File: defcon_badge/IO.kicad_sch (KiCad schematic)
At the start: 9 parts, among them J30 SAO 2x3, J31 microSD, J32 UART debug, SW20 TS-1187A, SW21 TS-1187A, SW22 TS-1187A, SW23 TS-1187A

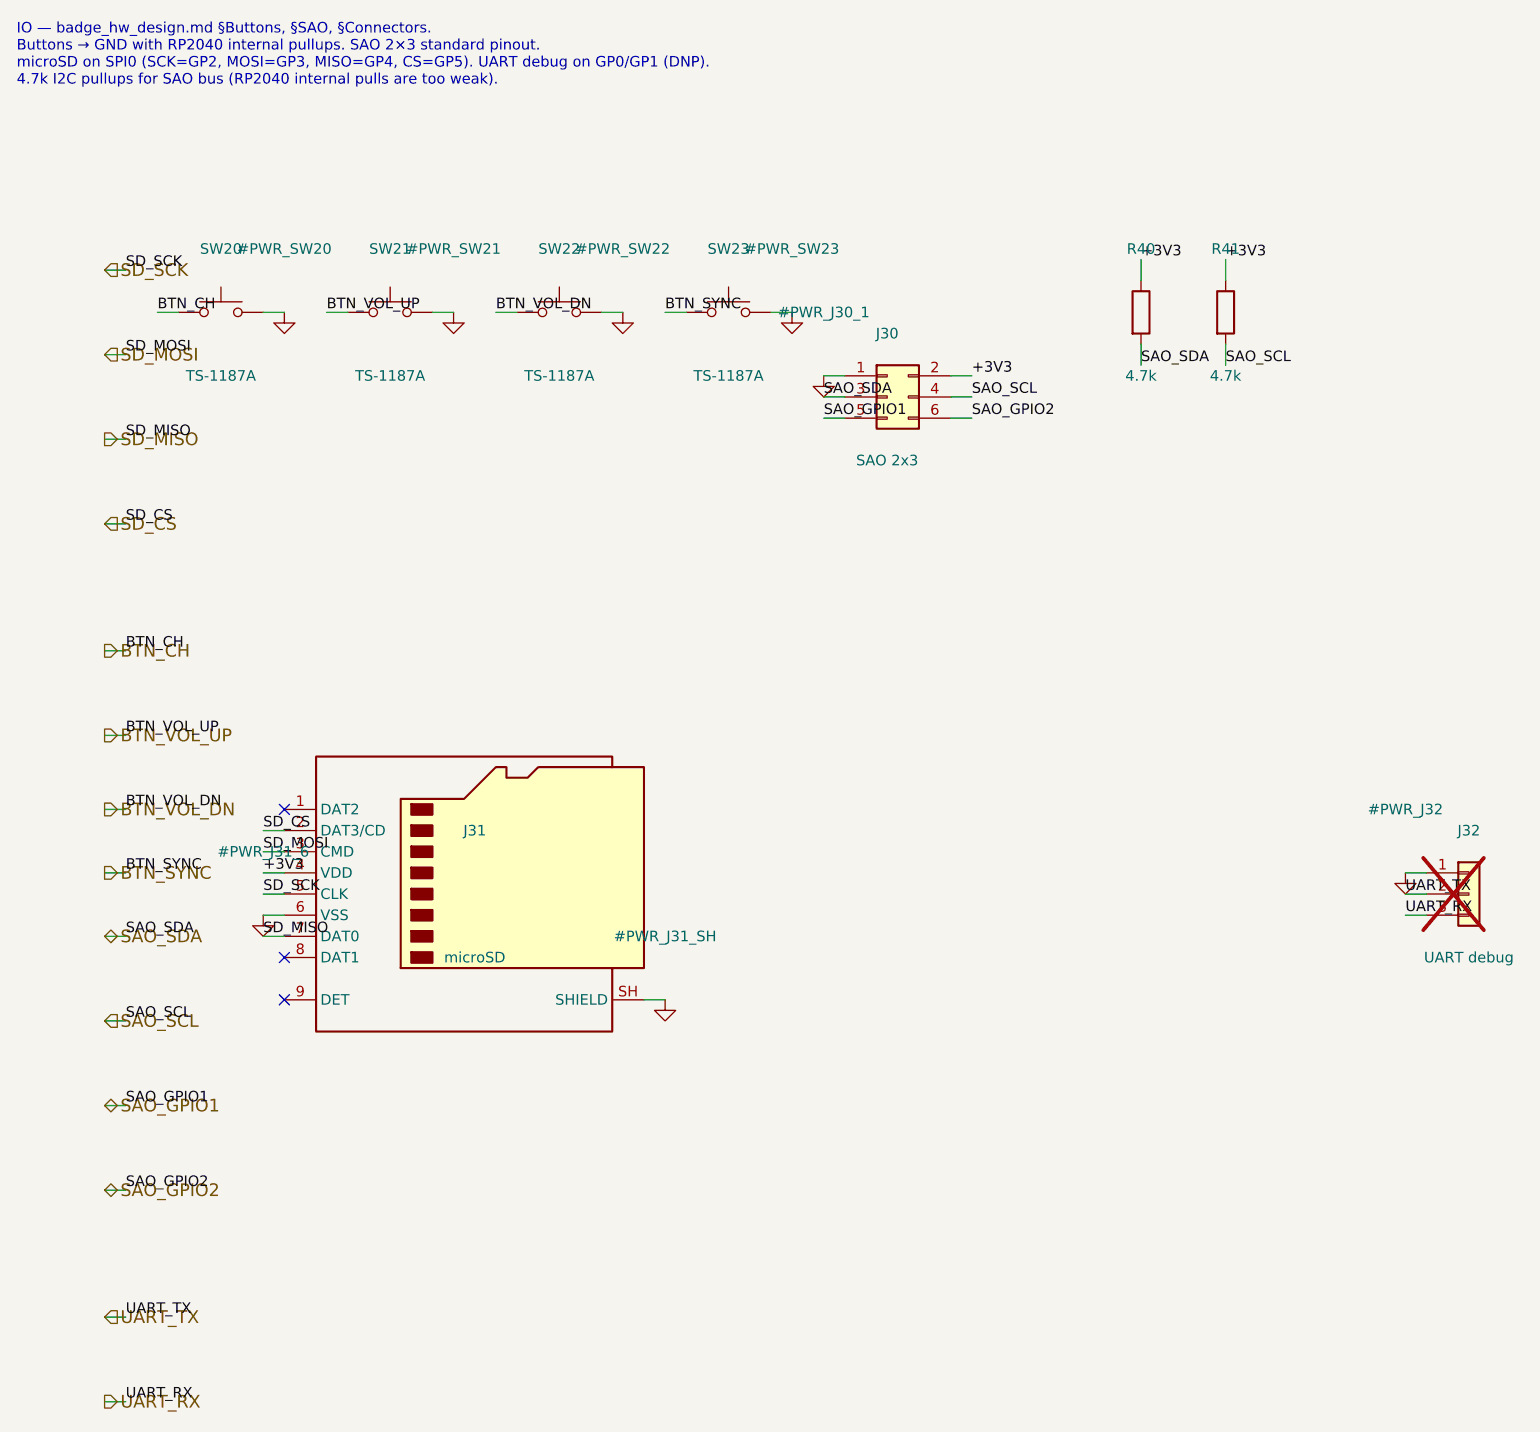
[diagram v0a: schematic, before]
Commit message: Schematic: fix +3V3 power-tree (board was dead) + add review framework
The +3V3 rail was fragmented into 5 disconnected nets — child sheets emitted it
via sheet-local (label "+3V3") while MCU_Core used global power:+3V3 symbols, so
the LDO output reached zero loads and the whole board could not power up
(6 ERC errors incl. 5 power_pin_not_driven). Root-caused and fixed at the
GENERATOR level, then regenerated the sheets:

- kicad_sheet_gen.py: RAIL_NAMES + label_at_pin() routes rail nets through the
  global power: symbol (never a sheet-local label that can't cross hierarchy).
- gen_power_sheet.py: add #FLG_GND PWR_FLAG (GND was undriven); drop redundant
  #FLG_BAT (it shorted two power outputs -> pin_to_pin error).
- gen_io_sheet.py: restore SW23 (SYNC button) + BTN_SYNC — caught generator drift
  where the committed schematic had SW23 but the generator only made 3 buttons.

Result (authoritative kicad-cli ERC/netlist): ERC 6->0 errors, +3V3 unified
(5 nets -> 1), all power pins driven, no pin conflicts. 4/5 gates pass (the 5th
is the 7 intentional RP2040 GPIO spares).

Adds schematic_phase/ — an authoritative, repeatable schematic-review framework
mirroring placement_phase_2/ (HARNESS, LEDGER, metrics.jsonl, and tools/sch_health.py
which derives all metrics from kicad-cli, not the analyzer that over-merges nets).

Co-Authored-By: Claude Opus 4.8 (1M context) <noreply@anthropic.com>
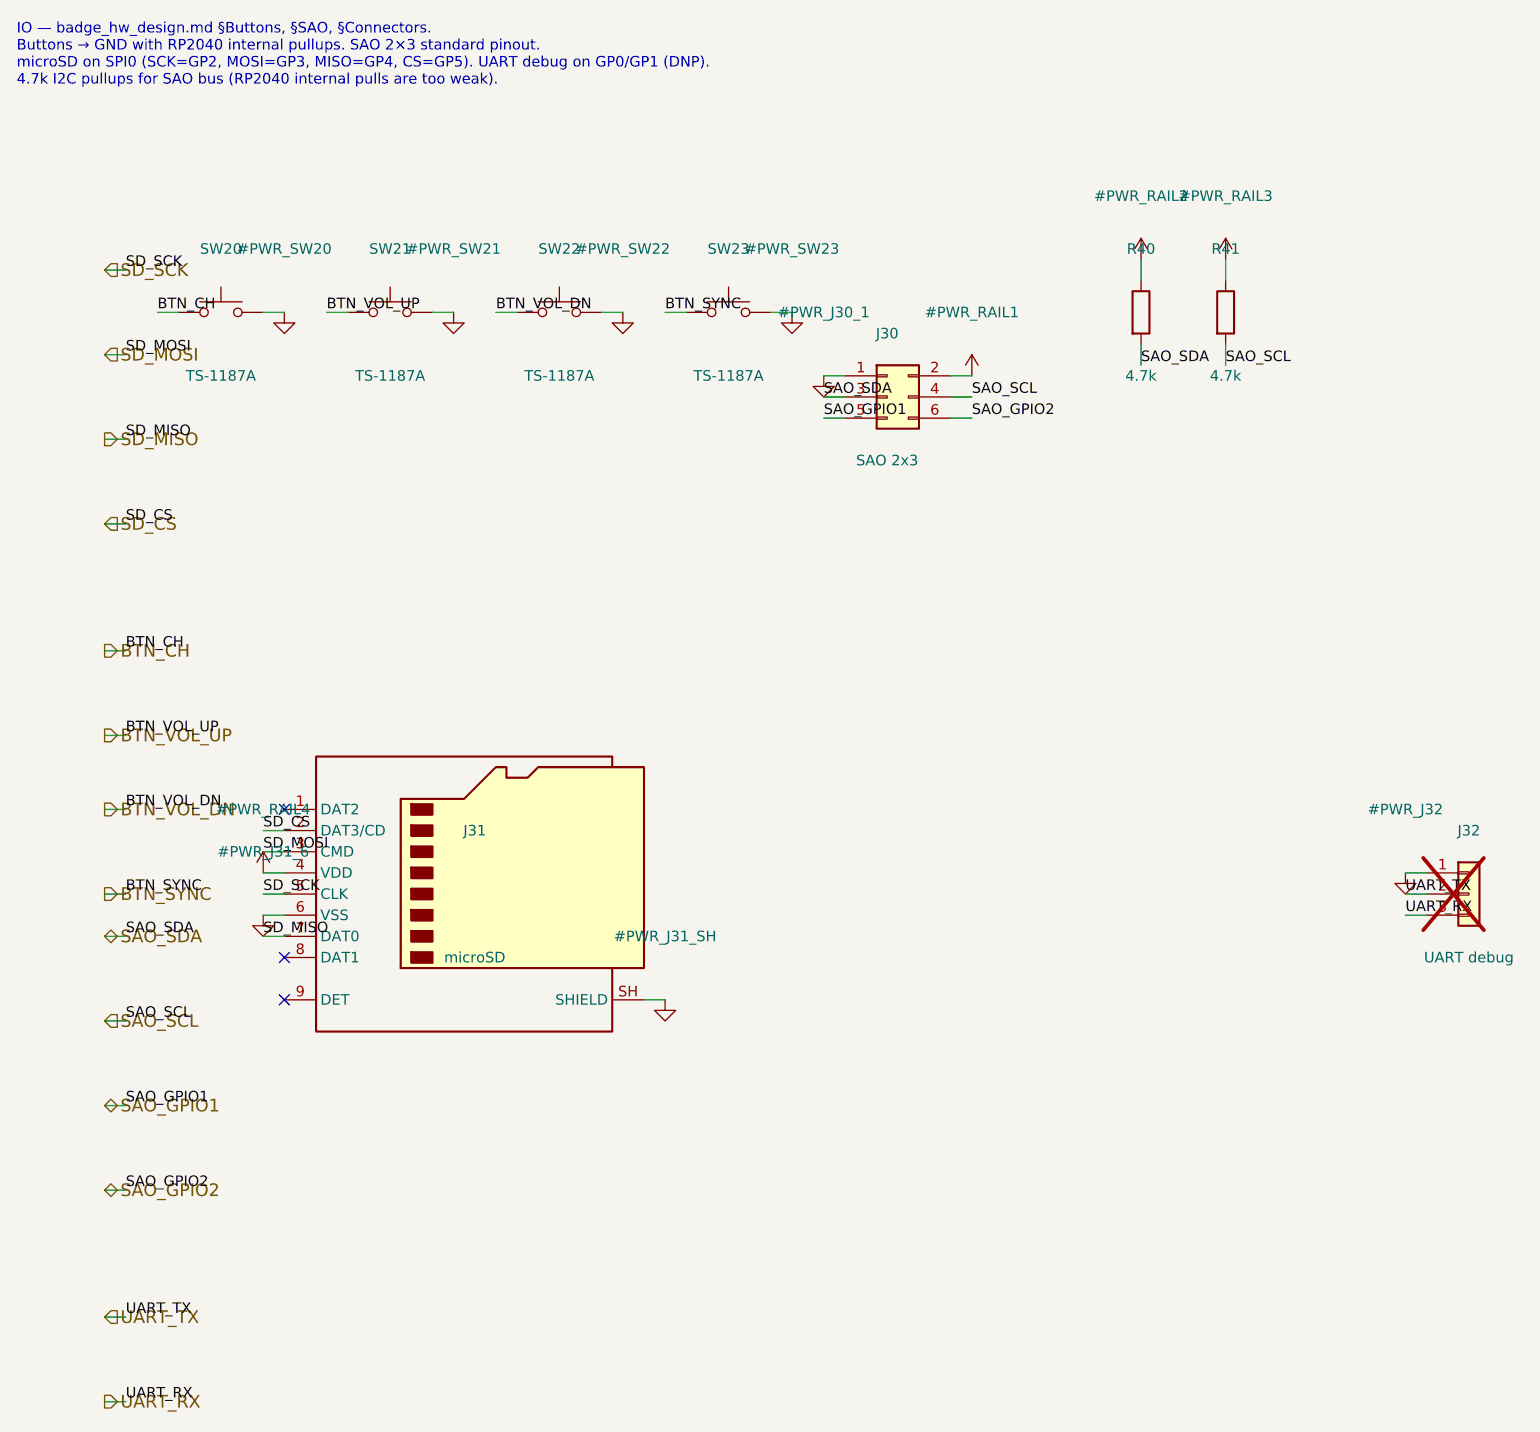
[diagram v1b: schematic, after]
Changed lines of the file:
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@@
 		(property "Footprint" "Button_Switch_SMD:SW_SPST_TL3342" (at 110.49 59.69 0) (show_name no) (hide yes) (effects (font (size 1.27 1.27))))
 		(property "Datasheet" "" (at 110.49 59.69 0) (show_name no) (hide yes) (effects (font (size 1.27 1.27))))
-		(property "Description" "Sync button (SYNC), 6mm tactile" (at 110.49 59.69 0) (show_name no) (hide yes) (effects (font (size 1.27 1.27))))
+		(property "Description" "Sync (tap-to-sync) button" (at 110.49 59.69 0) (show_name no) (hide yes) (effects (font (size 1.27 1.27))))
 		(property "MPN" "TS-1187A-B-A-B" (at 110.49 59.69 0) (show_name no) (hide yes) (effects (font (size 1.27 1.27))))
 		(property "LCSC" "C455257" (at 110.49 59.69 0) (show_name no) (hide yes) (effects (font (size 1.27 1.27))))
@@
 	)
 	(symbol
+		(lib_id "power:+3V3")
+		(at 139.70 67.31 0)
+		(unit 1)
+		(body_style 1)
+		(exclude_from_sim no)
+		(in_bom yes)
+		(on_board yes)
+		(in_pos_files yes)
+		(dnp no)
+		(fields_autoplaced yes)
+		(property "Reference" "#PWR_RAIL1" (at 139.70 59.69 0) (effects (font (size 1.27 1.27))))
+		(property "Value" "+3V3" (at 139.70 74.93 0) (effects (font (size 1.27 1.27)) (hide yes)))
+		(property "Footprint" "" (at 139.70 67.31 0) (show_name no) (hide yes) (effects (font (size 1.27 1.27))))
+		(property "Datasheet" "" (at 139.70 67.31 0) (show_name no) (hide yes) (effects (font (size 1.27 1.27))))
+		(property "Description" "" (at 139.70 67.31 0) (show_name no) (hide yes) (effects (font (size 1.27 1.27))))
+		(pin "1")
+		(instances
+			(project "defcon_badge"
+				(path "/8c0b3d8b-46d3-4173-ab1e-a61765f77d61/608539de-722a-4bca-b1da-2c313b60cd6f"
+					(reference "#PWR_RAIL1")
+					(unit 1)
+				)
+			)
+		)
+	)
+	(symbol
 		(lib_id "Device:R")
 		(at 160.02 59.69 0)
@@
 				(path "/8c0b3d8b-46d3-4173-ab1e-a61765f77d61/608539de-722a-4bca-b1da-2c313b60cd6f"
 					(reference "R41")
+					(unit 1)
+				)
+			)
+		)
+	)
+	(symbol
+		(lib_id "power:+3V3")
+		(at 160.02 53.34 0)
+		(unit 1)
+		(body_style 1)
+		(exclude_from_sim no)
+		(in_bom yes)
+		(on_board yes)
+		(in_pos_files yes)
+		(dnp no)
+		(fields_autoplaced yes)
+		(property "Reference" "#PWR_RAIL2" (at 160.02 45.72 0) (effects (font (size 1.27 1.27))))
+		(property "Value" "+3V3" (at 160.02 60.96 0) (effects (font (size 1.27 1.27)) (hide yes)))
+		(property "Footprint" "" (at 160.02 53.34 0) (show_name no) (hide yes) (effects (font (size 1.27 1.27))))
+		(property "Datasheet" "" (at 160.02 53.34 0) (show_name no) (hide yes) (effects (font (size 1.27 1.27))))
+		(property "Description" "" (at 160.02 53.34 0) (show_name no) (hide yes) (effects (font (size 1.27 1.27))))
+		(pin "1")
+		(instances
+			(project "defcon_badge"
+				(path "/8c0b3d8b-46d3-4173-ab1e-a61765f77d61/608539de-722a-4bca-b1da-2c313b60cd6f"
+					(reference "#PWR_RAIL2")
+					(unit 1)
+				)
+			)
+		)
+	)
+	(symbol
+		(lib_id "power:+3V3")
+		(at 170.18 53.34 0)
+		(unit 1)
+		(body_style 1)
+		(exclude_from_sim no)
+		(in_bom yes)
+		(on_board yes)
+		(in_pos_files yes)
+		(dnp no)
+		(fields_autoplaced yes)
+		(property "Reference" "#PWR_RAIL3" (at 170.18 45.72 0) (effects (font (size 1.27 1.27))))
+		(property "Value" "+3V3" (at 170.18 60.96 0) (effects (font (size 1.27 1.27)) (hide yes)))
+		(property "Footprint" "" (at 170.18 53.34 0) (show_name no) (hide yes) (effects (font (size 1.27 1.27))))
+		(property "Datasheet" "" (at 170.18 53.34 0) (show_name no) (hide yes) (effects (font (size 1.27 1.27))))
+		(property "Description" "" (at 170.18 53.34 0) (show_name no) (hide yes) (effects (font (size 1.27 1.27))))
+		(pin "1")
+		(instances
+			(project "defcon_badge"
+				(path "/8c0b3d8b-46d3-4173-ab1e-a61765f77d61/608539de-722a-4bca-b1da-2c313b60cd6f"
+					(reference "#PWR_RAIL3")
 					(unit 1)
 				)
@@
 				(path "/8c0b3d8b-46d3-4173-ab1e-a61765f77d61/608539de-722a-4bca-b1da-2c313b60cd6f"
 					(reference "J31")
+					(unit 1)
+				)
+			)
+		)
+	)
+	(symbol
+		(lib_id "power:+3V3")
+		(at 54.61 127.00 0)
+		(unit 1)
+		(body_style 1)
+		(exclude_from_sim no)
+		(in_bom yes)
+		(on_board yes)
+		(in_pos_files yes)
+		(dnp no)
+		(fields_autoplaced yes)
+		(property "Reference" "#PWR_RAIL4" (at 54.61 119.38 0) (effects (font (size 1.27 1.27))))
+		(property "Value" "+3V3" (at 54.61 134.62 0) (effects (font (size 1.27 1.27)) (hide yes)))
+		(property "Footprint" "" (at 54.61 127.00 0) (show_name no) (hide yes) (effects (font (size 1.27 1.27))))
+		(property "Datasheet" "" (at 54.61 127.00 0) (show_name no) (hide yes) (effects (font (size 1.27 1.27))))
+		(property "Description" "" (at 54.61 127.00 0) (show_name no) (hide yes) (effects (font (size 1.27 1.27))))
+		(pin "1")
+		(instances
+			(project "defcon_badge"
+				(path "/8c0b3d8b-46d3-4173-ab1e-a61765f77d61/608539de-722a-4bca-b1da-2c313b60cd6f"
+					(reference "#PWR_RAIL4")
 					(unit 1)
 				)
@@
 	(wire (pts (xy 35.56 110.49) (xy 38.10 110.49)) (stroke (width 0) (type default)))
 	(wire (pts (xy 35.56 119.38) (xy 38.10 119.38)) (stroke (width 0) (type default)))
-	(wire (pts (xy 35.56 127.00) (xy 38.10 127.00)) (stroke (width 0) (type default)))
+	(wire (pts (xy 35.56 129.54) (xy 38.10 129.54)) (stroke (width 0) (type default)))
 	(wire (pts (xy 35.56 134.62) (xy 38.10 134.62)) (stroke (width 0) (type default)))
 	(wire (pts (xy 35.56 144.78) (xy 38.10 144.78)) (stroke (width 0) (type default)))
@@
 	(label "BTN_VOL_DN" (at 82.55 59.69 0) (effects (font (size 1.27 1.27)) (justify left bottom)))
 	(label "BTN_SYNC" (at 102.87 59.69 0) (effects (font (size 1.27 1.27)) (justify left bottom)))
-	(label "+3V3" (at 139.70 67.31 0) (effects (font (size 1.27 1.27)) (justify left bottom)))
 	(label "SAO_SDA" (at 121.92 69.85 0) (effects (font (size 1.27 1.27)) (justify left bottom)))
 	(label "SAO_SCL" (at 139.70 69.85 0) (effects (font (size 1.27 1.27)) (justify left bottom)))
 	(label "SAO_GPIO1" (at 121.92 72.39 0) (effects (font (size 1.27 1.27)) (justify left bottom)))
 	(label "SAO_GPIO2" (at 139.70 72.39 0) (effects (font (size 1.27 1.27)) (justify left bottom)))
-	(label "+3V3" (at 160.02 53.34 0) (effects (font (size 1.27 1.27)) (justify left bottom)))
 	(label "SAO_SDA" (at 160.02 66.04 0) (effects (font (size 1.27 1.27)) (justify left bottom)))
-	(label "+3V3" (at 170.18 53.34 0) (effects (font (size 1.27 1.27)) (justify left bottom)))
 	(label "SAO_SCL" (at 170.18 66.04 0) (effects (font (size 1.27 1.27)) (justify left bottom)))
 	(label "SD_CS" (at 54.61 121.92 0) (effects (font (size 1.27 1.27)) (justify left bottom)))
 	(label "SD_MOSI" (at 54.61 124.46 0) (effects (font (size 1.27 1.27)) (justify left bottom)))
-	(label "+3V3" (at 54.61 127.00 0) (effects (font (size 1.27 1.27)) (justify left bottom)))
 	(label "SD_SCK" (at 54.61 129.54 0) (effects (font (size 1.27 1.27)) (justify left bottom)))
 	(label "SD_MISO" (at 54.61 134.62 0) (effects (font (size 1.27 1.27)) (justify left bottom)))
@@
 	(label "BTN_VOL_UP" (at 38.10 110.49 0) (effects (font (size 1.27 1.27)) (justify left bottom)))
 	(label "BTN_VOL_DN" (at 38.10 119.38 0) (effects (font (size 1.27 1.27)) (justify left bottom)))
-	(label "BTN_SYNC" (at 38.10 127.00 0) (effects (font (size 1.27 1.27)) (justify left bottom)))
+	(label "BTN_SYNC" (at 38.10 129.54 0) (effects (font (size 1.27 1.27)) (justify left bottom)))
 	(label "SAO_SDA" (at 38.10 134.62 0) (effects (font (size 1.27 1.27)) (justify left bottom)))
 	(label "SAO_SCL" (at 38.10 144.78 0) (effects (font (size 1.27 1.27)) (justify left bottom)))
@@
 	(hierarchical_label "BTN_VOL_UP" (shape output) (at 35.56 110.49 0) (effects (font (size 1.524 1.524)) (justify left)))
 	(hierarchical_label "BTN_VOL_DN" (shape output) (at 35.56 119.38 0) (effects (font (size 1.524 1.524)) (justify left)))
-	(hierarchical_label "BTN_SYNC" (shape output) (at 35.56 127.00 0) (effects (font (size 1.524 1.524)) (justify left)))
+	(hierarchical_label "BTN_SYNC" (shape output) (at 35.56 129.54 0) (effects (font (size 1.524 1.524)) (justify left)))
 	(hierarchical_label "SAO_SDA" (shape bidirectional) (at 35.56 134.62 0) (effects (font (size 1.524 1.524)) (justify left)))
 	(hierarchical_label "SAO_SCL" (shape input) (at 35.56 144.78 0) (effects (font (size 1.524 1.524)) (justify left)))
